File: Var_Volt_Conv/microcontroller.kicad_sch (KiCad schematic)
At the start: 14 parts, among them J201 Conn_01x05, SW201 SW_Push, U201 STM32G030F6Px, Y201 16MHz

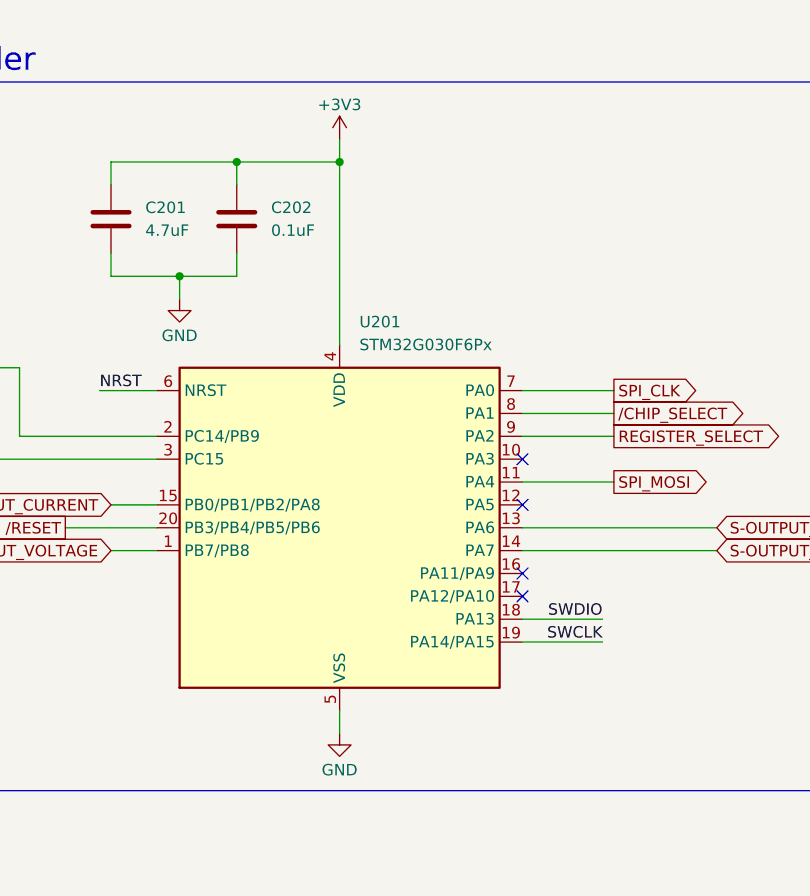
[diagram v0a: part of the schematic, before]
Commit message: Fixed ERC issues
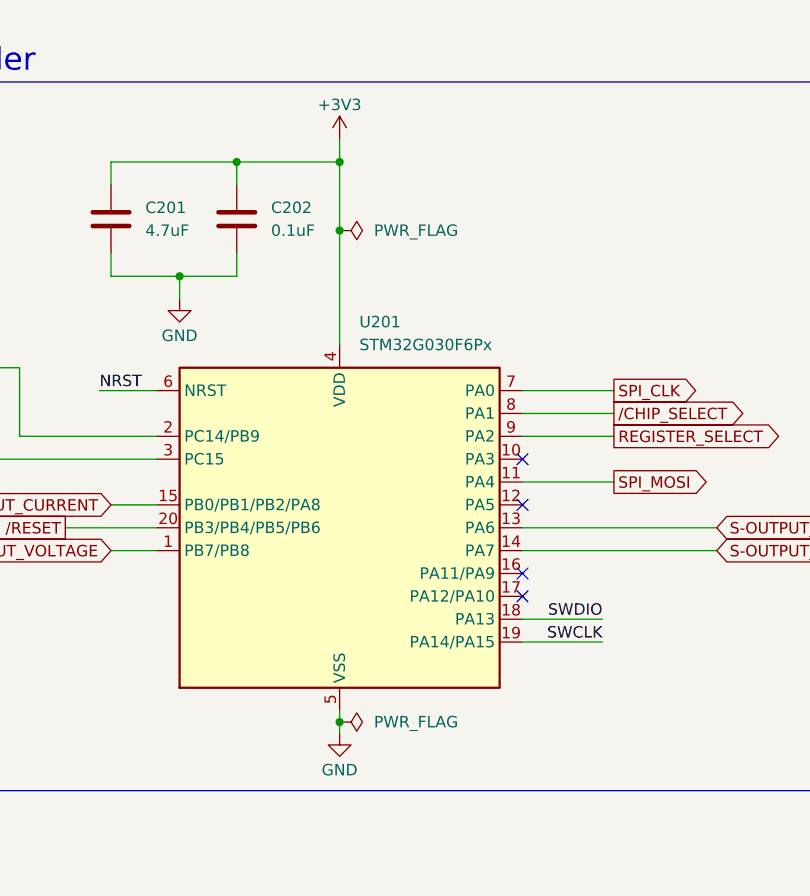
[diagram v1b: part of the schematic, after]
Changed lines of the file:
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@@
+	)
+	(junction
+		(at 156.21 50.8)
+		(diameter 0)
+		(color 0 0 0 0)
+	)
+	(junction
+		(at 156.21 105.41)
+		(diameter 0)
+		(color 0 0 0 0)
 	)
 	(junction
@@
 	(wire
 		(pts
-			(xy 156.21 43.18) (xy 156.21 63.5)
+			(xy 156.21 43.18) (xy 156.21 50.8)
 		)
 		(stroke
@@
 	(wire
 		(pts
+			(xy 156.21 50.8) (xy 156.21 63.5)
+		)
+		(stroke
+			(width 0)
+			(type default)
+		)
+	)
+	(wire
+		(pts
 			(xy 74.93 87.63) (xy 74.93 74.93)
 		)
@@
 	(wire
 		(pts
-			(xy 156.21 104.14) (xy 156.21 106.68)
+			(xy 156.21 104.14) (xy 156.21 105.41)
 		)
 		(stroke
@@
 		(pts
 			(xy 148.59 144.78) (xy 154.94 144.78)
+		)
+		(stroke
+			(width 0)
+			(type default)
+		)
+	)
+	(wire
+		(pts
+			(xy 156.21 105.41) (xy 156.21 106.68)
 		)
 		(stroke
@@
 	)
 	(symbol
+		(lib_id "power:PWR_FLAG")
+		(at 156.21 50.8 270)
+		(unit 1)
+		(exclude_from_sim no)
+		(in_bom yes)
+		(on_board yes)
+		(dnp no)
+		(fields_autoplaced yes)
+		(property "Reference" "#FLG0405"
+			(at 158.115 50.8 0)
+			(effects
+				(font
+					(size 1.27 1.27)
+				)
+				(hide yes)
+			)
+		)
+		(property "Value" "PWR_FLAG"
+			(at 160.02 50.7999 90)
+			(effects
+				(font
+					(size 1.27 1.27)
+				)
+				(justify left)
+			)
+		)
+		(property "Footprint" ""
+			(at 156.21 50.8 0)
+			(effects
+				(font
+					(size 1.27 1.27)
+				)
+				(hide yes)
+			)
+		)
+		(property "Datasheet" "~"
+			(at 156.21 50.8 0)
+			(effects
+				(font
+					(size 1.27 1.27)
+				)
+				(hide yes)
+			)
+		)
+		(property "Description" "Special symbol for telling ERC where power comes from"
+			(at 156.21 50.8 0)
+			(effects
+				(font
+					(size 1.27 1.27)
+				)
+				(hide yes)
+			)
+		)
+		(pin "1"
+		)
+		(instances
+			(project "Var_Volt_Conv"
+				(path "/7c9580d6-c22f-4506-b9c3-9272e882c9fb/b048280b-6fef-4656-96bb-ca0a0c35ac5b"
+					(reference "#FLG0405")
+					(unit 1)
+				)
+			)
+		)
+	)
+	(symbol
 		(lib_id "Switch:SW_Push")
 		(at 59.69 148.59 90)
@@
 					(unit 1)
 				)
+			)
+		)
+	)
+	(symbol
+		(lib_id "power:PWR_FLAG")
+		(at 156.21 105.41 270)
+		(unit 1)
+		(exclude_from_sim no)
+		(in_bom yes)
+		(on_board yes)
+		(dnp no)
+		(fields_autoplaced yes)
+		(property "Reference" "#FLG0301"
+			(at 158.115 105.41 0)
+			(effects
+				(font
+					(size 1.27 1.27)
+				)
+				(hide yes)
+			)
+		)
+		(property "Value" "PWR_FLAG"
+			(at 160.02 105.4099 90)
+			(effects
+				(font
+					(size 1.27 1.27)
+				)
+				(justify left)
+			)
+		)
+		(property "Footprint" ""
+			(at 156.21 105.41 0)
+			(effects
+				(font
+					(size 1.27 1.27)
+				)
+				(hide yes)
+			)
+		)
+		(property "Datasheet" "~"
+			(at 156.21 105.41 0)
+			(effects
+				(font
+					(size 1.27 1.27)
+				)
+				(hide yes)
+			)
+		)
+		(property "Description" "Special symbol for telling ERC where power comes from"
+			(at 156.21 105.41 0)
+			(effects
+				(font
+					(size 1.27 1.27)
+				)
+				(hide yes)
+			)
+		)
+		(pin "1"
+		)
+		(instances
+			(project "Var_Volt_Conv"
+				(path "/7c9580d6-c22f-4506-b9c3-9272e882c9fb/b048280b-6fef-4656-96bb-ca0a0c35ac5b"
+					(reference "#FLG0301")
+					(unit 1)
+				)

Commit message: Add footprints and correct LCD pin numbering
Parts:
- D201, D202, D203, D204: footprint (none) -> Diode_SMD:D_SOD-323
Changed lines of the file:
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@@
 			)
 		)
-		(property "Footprint" ""
+		(property "Footprint" "Diode_SMD:D_SOD-323"
 			(at 162.56 162.56 0)
 			(effects
@@
 			)
 		)
-		(property "Footprint" ""
+		(property "Footprint" "Diode_SMD:D_SOD-323"
 			(at 134.62 162.56 0)
 			(effects
@@
 			)
 		)
-		(property "Footprint" ""
+		(property "Footprint" "Diode_SMD:D_SOD-323"
 			(at 148.59 162.56 0)
 			(effects
@@
 			)
 		)
-		(property "Footprint" ""
+		(property "Footprint" "Diode_SMD:D_SOD-323"
 			(at 120.65 162.56 0)
 			(effects

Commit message: Add footprints for all capacitors, and record cap part names
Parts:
- C201: footprint (none) -> Capacitor_SMD:C_0603_1608Metric
- C202, C203, C204, C205: footprint (none) -> Capacitor_SMD:C_0402_1005Metric
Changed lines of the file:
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@@
 			)
 		)
-		(property "Footprint" ""
+		(property "Footprint" "Capacitor_SMD:C_0603_1608Metric"
 			(at 131.7752 53.34 0)
 			(effects
@@
 			)
 		)
-		(property "Footprint" ""
+		(property "Footprint" "Capacitor_SMD:C_0402_1005Metric"
 			(at 88.9 65.0748 0)
 			(effects
@@
 			)
 		)
-		(property "Footprint" ""
+		(property "Footprint" "Capacitor_SMD:C_0402_1005Metric"
 			(at 88.9 86.6648 0)
 			(effects
@@
 			)
 		)
-		(property "Footprint" ""
+		(property "Footprint" "Capacitor_SMD:C_0402_1005Metric"
 			(at 145.7452 53.34 0)
 			(effects
@@
 			)
 		)
-		(property "Footprint" ""
+		(property "Footprint" "Capacitor_SMD:C_0402_1005Metric"
 			(at 73.3552 152.4 0)
 			(effects

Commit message: Add inductor footprint
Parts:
- Y201: footprint (none) -> Crystal:Crystal_SMD_3225-4Pin_3.2x2.5mm
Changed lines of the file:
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@@
 			)
 		)
-		(property "Footprint" ""
+		(property "Footprint" "Crystal:Crystal_SMD_3225-4Pin_3.2x2.5mm"
 			(at 96.52 74.93 0)
 			(effects

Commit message: Added footprints to all components except the connectors and buck-boost converter
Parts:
- R201: footprint (none) -> Resistor_SMD:R_0603_1608Metric
- SW201: footprint (none) -> Button_Switch_SMD:SW_Tactile_SPST_NO_Straight_CK_PTS636Sx25SMTRLFS
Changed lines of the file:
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@@
 			)
 		)
-		(property "Footprint" ""
+		(property "Footprint" "Button_Switch_SMD:SW_Tactile_SPST_NO_Straight_CK_PTS636Sx25SMTRLFS"
 			(at 54.61 148.59 0)
 			(effects
@@
 			)
 		)
-		(property "Footprint" ""
+		(property "Footprint" "Resistor_SMD:R_0603_1608Metric"
 			(at 102.87 84.328 90)
 			(effects

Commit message: Assign footprints to all footprints except the buck-boost converter
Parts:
- J201: footprint (none) -> Connector_PinHeader_2.54mm:PinHeader_1x05_P2.54mm_Vertical
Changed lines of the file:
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@@
 			)
 		)
-		(property "Footprint" ""
+		(property "Footprint" "Connector_PinHeader_2.54mm:PinHeader_1x05_P2.54mm_Vertical"
 			(at 104.14 147.32 0)
 			(effects

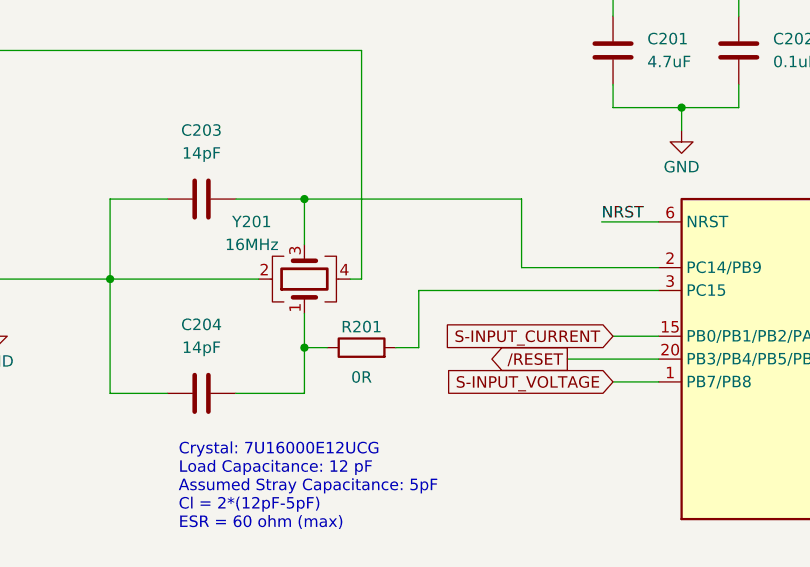
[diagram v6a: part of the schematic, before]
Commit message: Completed rough layout
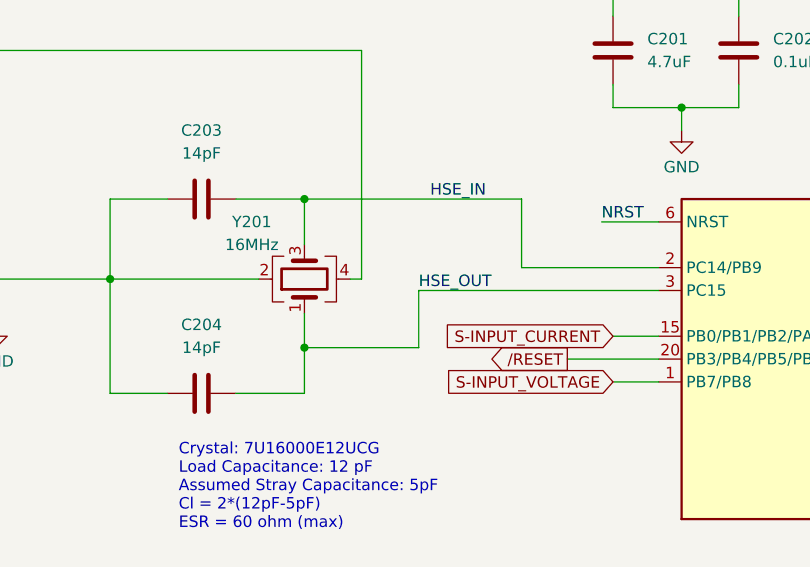
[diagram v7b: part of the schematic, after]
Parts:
- removed R201: 0R, Resistor_SMD:R_0603_1608Metric, symbol Device:R
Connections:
- net HSE_IN: now reaches C203.2, U201.2 (PC14/PB9), Y201.3
- net HSE_OUT: now reaches C204.2, Y201.1
- net HSE_OUT: now also U201.3 (PC15)
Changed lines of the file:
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@@
 	(wire
 		(pts
-			(xy 96.52 82.55) (xy 99.06 82.55)
+			(xy 96.52 82.55) (xy 109.22 82.55)
 		)
 		(stroke
@@
 		(pts
 			(xy 162.56 166.37) (xy 162.56 172.72)
-		)
-		(stroke
-			(width 0)
-			(type default)
-		)
-	)
-	(wire
-		(pts
-			(xy 106.68 82.55) (xy 109.22 82.55)
 		)
 		(stroke
@@
 		)
 	)
+	(label "HSE_OUT"
+		(at 109.22 76.2 0)
+		(fields_autoplaced yes)
+		(effects
+			(font
+				(size 1.27 1.27)
+			)
+			(justify left bottom)
+		)
+	)
 	(label "SWCLK"
 		(at 185.42 96.52 180)
@@
 			)
 			(justify right bottom)
+		)
+	)
+	(label "HSE_IN"
+		(at 110.49 66.04 0)
+		(fields_autoplaced yes)
+		(effects
+			(font
+				(size 1.27 1.27)
+			)
+			(justify left bottom)
 		)
 	)
@@
 					(unit 1)
 				)
-			)
-		)
-	)
-	(symbol
-		(lib_id "Device:R")
-		(at 102.87 82.55 90)
-		(unit 1)
-		(exclude_from_sim no)
-		(in_bom yes)
-		(on_board yes)
-		(dnp no)
-		(property "Reference" "R201"
-			(at 102.87 80.264 90)
-			(effects
-				(font
-					(size 1.27 1.27)
-				)
-			)
-		)
-		(property "Value" "0R"
-			(at 102.87 85.852 90)
-			(effects
-				(font
-					(size 1.27 1.27)
-				)
-			)
-		)
-		(property "Footprint" "Resistor_SMD:R_0603_1608Metric"
-			(at 102.87 84.328 90)
-			(effects
-				(font
-					(size 1.27 1.27)
-				)
-				(hide yes)
-			)
-		)
-		(property "Datasheet" "~"
-			(at 102.87 82.55 0)
-			(effects
-				(font
-					(size 1.27 1.27)
-				)
-				(hide yes)
-			)
-		)
-		(property "Description" "Resistor"
-			(at 102.87 82.55 0)
-			(effects
-				(font
-					(size 1.27 1.27)
-				)
-				(hide yes)
-			)
-		)
-		(pin "1"
-		)
-		(pin "2"
-		)
-		(instances
-			(project ""
-				(path "/7c9580d6-c22f-4506-b9c3-9272e882c9fb/b048280b-6fef-4656-96bb-ca0a0c35ac5b"
-					(reference "R201")
-					(unit 1)
-				)

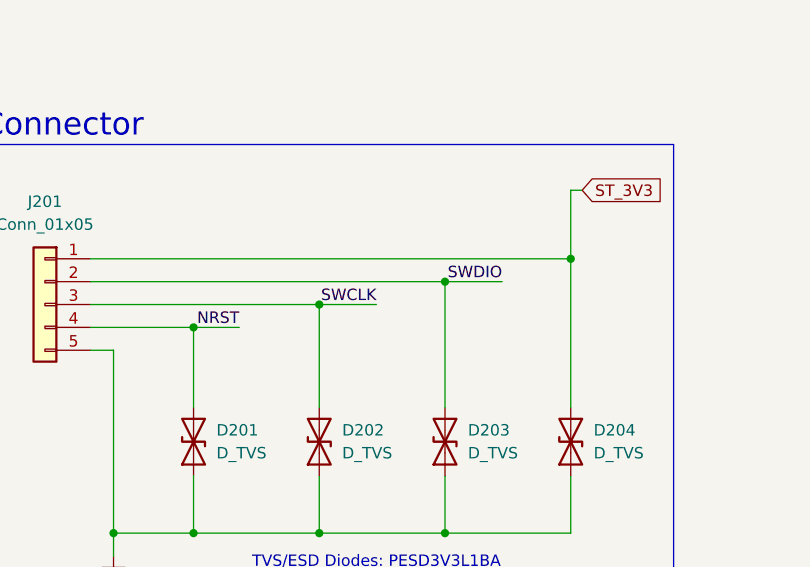
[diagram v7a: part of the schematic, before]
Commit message: Routed signal traces and made power pours for microcontroller and display, also changed 4.7, 1uF and 2.2uF caps to 0402
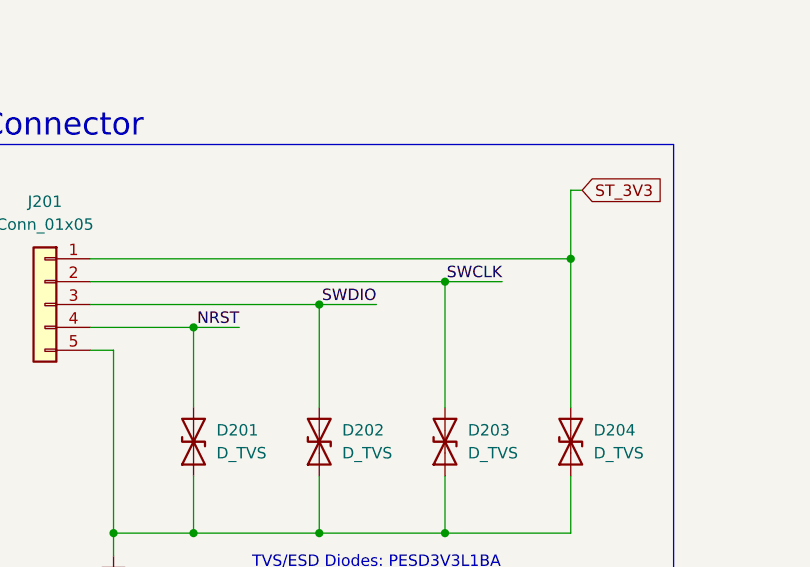
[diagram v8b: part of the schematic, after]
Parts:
- C201: footprint Capacitor_SMD:C_0603_1608Metric -> Capacitor_SMD:C_0402_1005Metric
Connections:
- net SWCLK: now also D203.2 (A2), J201.2 (Pin_2); no longer D202.2 (A2), J201.3 (Pin_3)
- net SWDIO: now also D202.2 (A2), J201.3 (Pin_3); no longer D203.2 (A2), J201.2 (Pin_2)
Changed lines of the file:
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@@
 		)
 	)
-	(label "SWCLK"
+	(label "SWDIO"
 		(at 140.97 147.32 180)
 		(fields_autoplaced yes)
@@
 		)
 	)
-	(label "SWDIO"
+	(label "SWCLK"
 		(at 154.94 144.78 180)
 		(fields_autoplaced yes)
@@
 			)
 		)
-		(property "Footprint" "Capacitor_SMD:C_0603_1608Metric"
+		(property "Footprint" "Capacitor_SMD:C_0402_1005Metric"
 			(at 131.7752 53.34 0)
 			(effects
